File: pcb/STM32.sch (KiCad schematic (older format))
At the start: 34 parts

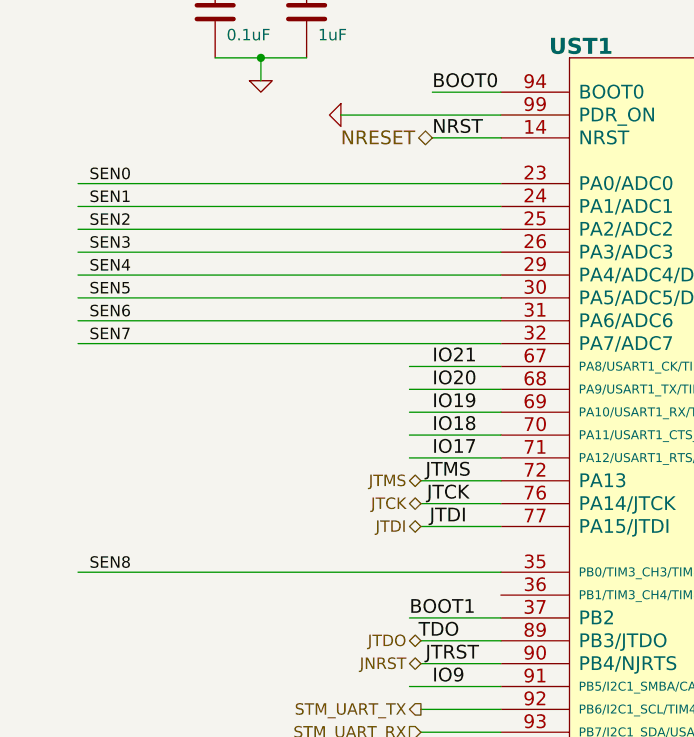
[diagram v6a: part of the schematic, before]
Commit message: analog signals routed
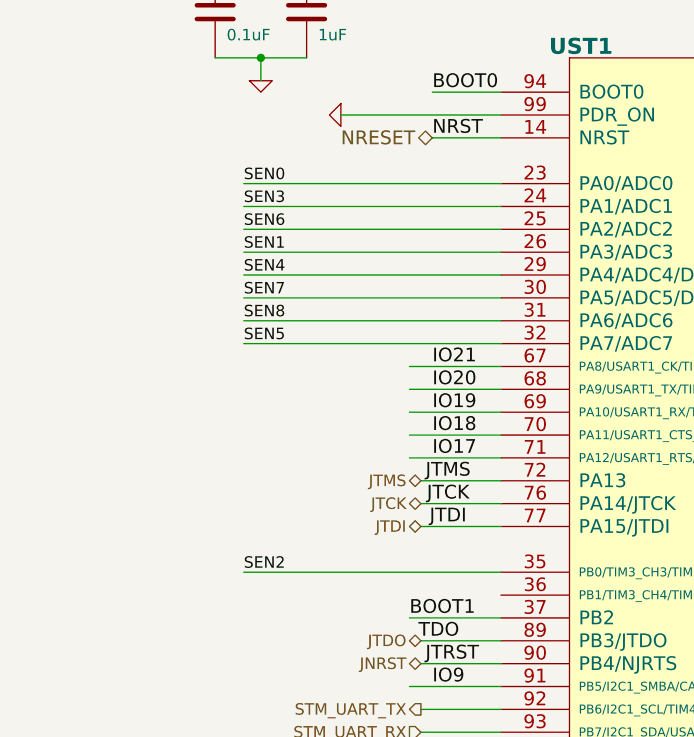
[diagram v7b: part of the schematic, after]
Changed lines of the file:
@@
 Text HLabel 2300 1600 0    60   BiDi ~ 0
 NRESET
-Text Label 800  2400 0    50   ~ 0
+Text Label 1475 2000 0    50   ~ 0
 SEN6
-Text Label 800  2300 0    50   ~ 0
+Text Label 1475 2500 0    50   ~ 0
 SEN5
-Text Label 800  2200 0    50   ~ 0
+Text Label 1475 2200 0    50   ~ 0
 SEN4
-Text Label 800  2100 0    50   ~ 0
+Text Label 1475 1900 0    50   ~ 0
 SEN3
-Text Label 800  2000 0    50   ~ 0
+Text Label 1475 3500 0    50   ~ 0
 SEN2
-Text Label 800  1900 0    50   ~ 0
+Text Label 1475 2100 0    50   ~ 0
 SEN1
 Text Label 2504 3900 2    60   ~ 0
@@
 Text Label 2200 3700 0    60   ~ 0
 BOOT1
-Text Label 800  1800 0    50   ~ 0
+Text Label 1475 1800 0    50   ~ 0
 SEN0
 $Comp
@@
 Text HLabel 6050 2850 2    50   BiDi ~ 0
 PE[0..7]
-Text Label 800  3500 0    50   ~ 0
+Text Label 1475 2400 0    50   ~ 0
 SEN8
-Text Label 800  2500 0    50   ~ 0
+Text Label 1475 2300 0    50   ~ 0
 SEN7
 Text Label 8600 2000 0    50   ~ 0
@@
 SEN[0..8]
 Wire Wire Line
-	750  3500 2600 3500
-Wire Wire Line
-	750  1800 2600 1800
-Wire Wire Line
-	750  1900 2600 1900
-Wire Wire Line
-	750  2000 2600 2000
-Wire Wire Line
-	750  2100 2600 2100
-Wire Wire Line
-	750  2200 2600 2200
-Wire Wire Line
-	750  2300 2600 2300
-Wire Wire Line
-	750  2400 2600 2400
-Wire Wire Line
-	750  2500 2600 2500
+	1475 3500 2600 3500
+Wire Wire Line
+	1475 1800 2600 1800
+Wire Wire Line
+	1475 1900 2600 1900
+Wire Wire Line
+	1475 2000 2600 2000
+Wire Wire Line
+	1475 2100 2600 2100
+Wire Wire Line
+	1475 2200 2600 2200
+Wire Wire Line
+	1475 2300 2600 2300
+Wire Wire Line
+	1475 2400 2600 2400
+Wire Wire Line
+	1475 2500 2600 2500
 Wire Bus Line
 	5950 2850 5950 3550

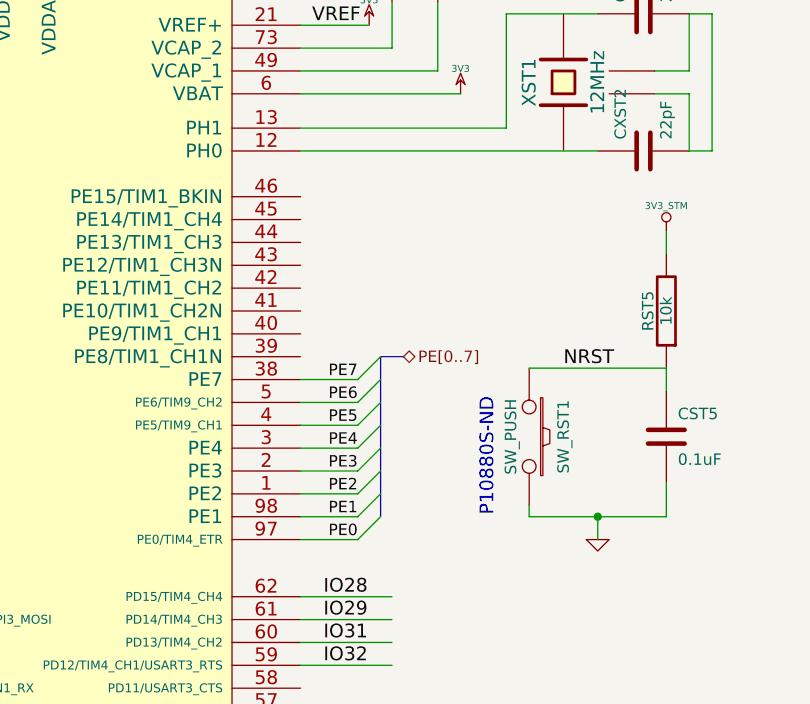
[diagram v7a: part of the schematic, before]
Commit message: solid state stm32's signals connected
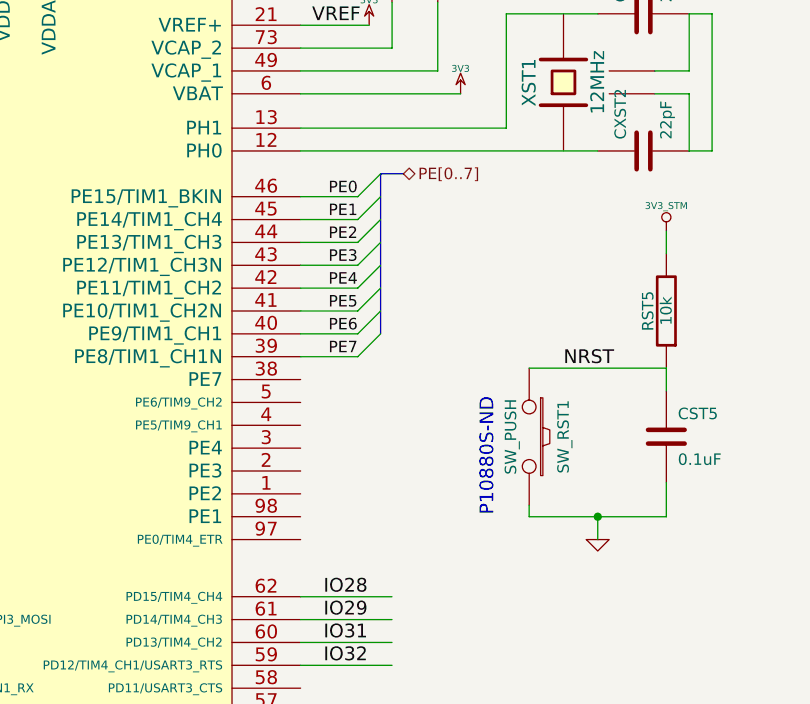
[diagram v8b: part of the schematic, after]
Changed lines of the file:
@@
 	5700 6100 5600 6100
 Wire Wire Line
-	5600 3650 5850 3650
+	5600 2150 5850 2150
 Entry Wire Line
-	5850 3650 5950 3550
+	5850 2850 5950 2750
 Wire Wire Line
-	5600 3550 5850 3550
+	5600 2250 5850 2250
 Entry Wire Line
-	5850 3550 5950 3450
-Text Label 5850 3650 2    50   ~ 0
+	5850 2750 5950 2650
+Text Label 5850 2150 2    50   ~ 0
 PE0
-Text Label 5850 3550 2    50   ~ 0
+Text Label 5850 2250 2    50   ~ 0
 PE1
 Wire Wire Line
-	5600 3450 5850 3450
+	5600 2350 5850 2350
 Entry Wire Line
-	5850 3450 5950 3350
+	5850 2650 5950 2550
 Wire Wire Line
-	5600 3350 5850 3350
+	5600 2450 5850 2450
 Entry Wire Line
-	5850 3350 5950 3250
-Text Label 5850 3450 2    50   ~ 0
+	5850 2550 5950 2450
+Text Label 5850 2350 2    50   ~ 0
 PE2
-Text Label 5850 3350 2    50   ~ 0
+Text Label 5850 2450 2    50   ~ 0
 PE3
 Wire Wire Line
-	5600 3250 5850 3250
+	5600 2550 5850 2550
 Entry Wire Line
-	5850 3250 5950 3150
+	5850 2450 5950 2350
 Wire Wire Line
-	5600 3150 5850 3150
+	5600 2650 5850 2650
 Entry Wire Line
-	5850 3150 5950 3050
-Text Label 5850 3250 2    50   ~ 0
+	5850 2350 5950 2250
+Text Label 5850 2550 2    50   ~ 0
 PE4
-Text Label 5850 3150 2    50   ~ 0
+Text Label 5850 2650 2    50   ~ 0
 PE5
 Wire Wire Line
-	5600 3050 5850 3050
+	5600 2750 5850 2750
 Entry Wire Line
-	5850 3050 5950 2950
+	5850 2250 5950 2150
 Wire Wire Line
-	5600 2950 5850 2950
+	5600 2850 5850 2850
 Entry Wire Line
-	5850 2950 5950 2850
-Text Label 5850 3050 2    50   ~ 0
+	5850 2150 5950 2050
+Text Label 5850 2750 2    50   ~ 0
 PE6
-Text Label 5850 2950 2    50   ~ 0
+Text Label 5850 2850 2    50   ~ 0
 PE7
 Wire Bus Line
-	5950 2850 6050 2850
-Text HLabel 6050 2850 2    50   BiDi ~ 0
+	5950 2050 6050 2050
+Text HLabel 6050 2050 2    50   BiDi ~ 0
 PE[0..7]
 Text Label 1475 2400 0    50   ~ 0
@@
 	1475 2500 2600 2500
 Wire Bus Line
-	5950 2850 5950 3550
+	5950 2050 5950 2750
 Wire Bus Line
 	8950 1300 8950 2100
